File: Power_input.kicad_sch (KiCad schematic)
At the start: 10 parts, among them J12 DG390-5.0-02P

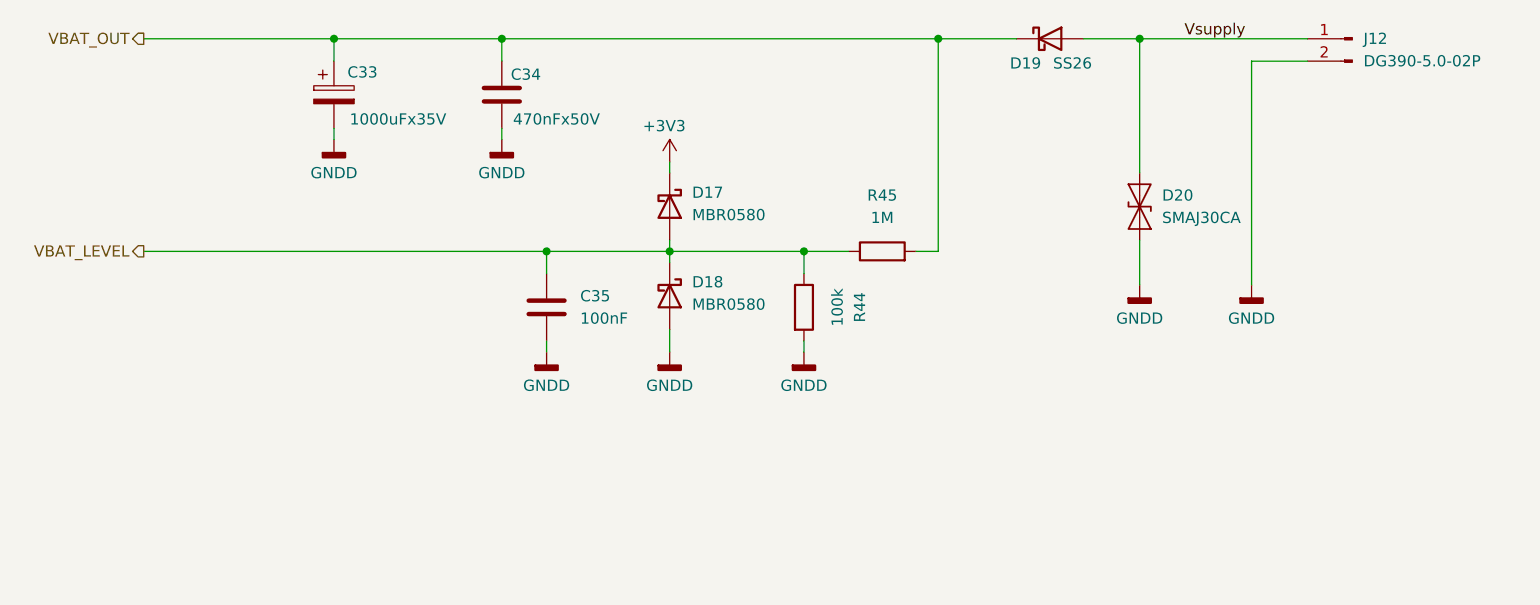
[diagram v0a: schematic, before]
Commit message: Dual SIM version
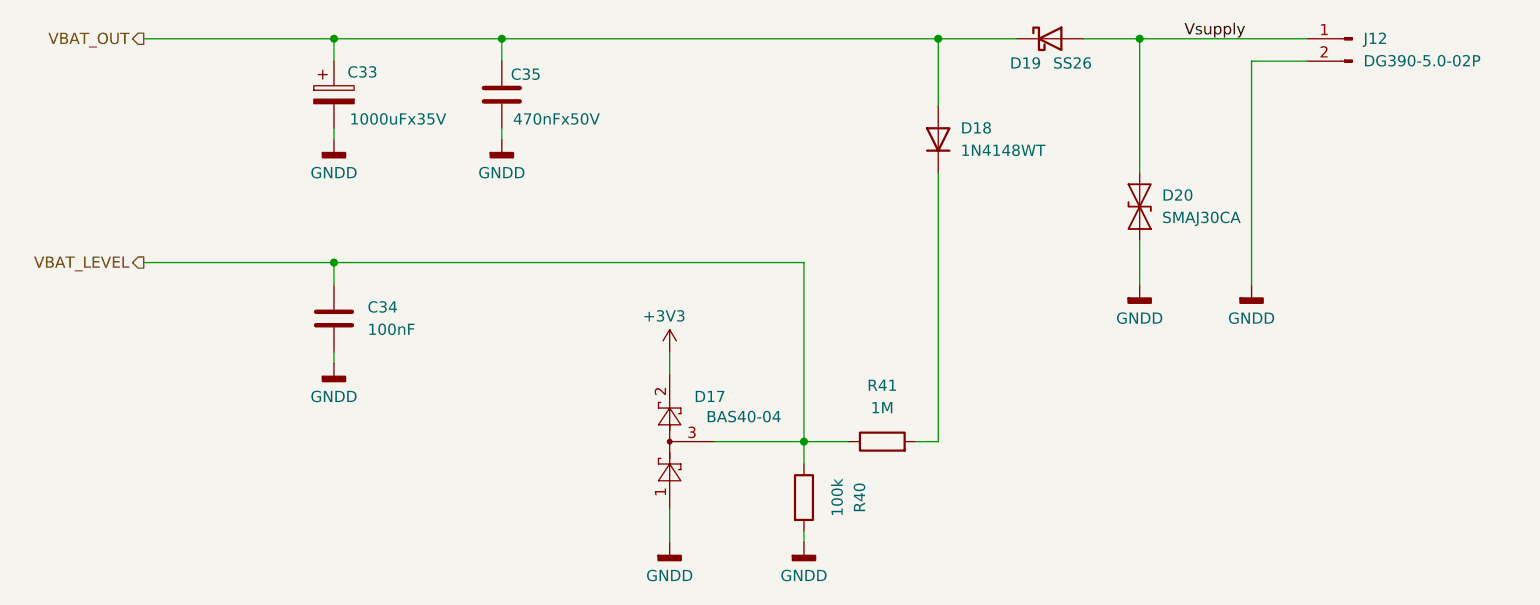
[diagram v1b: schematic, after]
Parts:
- removed D17, D18: MBR0580, Diode_SMD:D_SOD-123, symbol Diode:MBR0580
- added D17: BAS40-04, Package_TO_SOT_SMD:SOT-23, symbol Diode:BAS40-04
- added D18: 1N4148WT, Diode_SMD:D_SOD-523, symbol Diode:1N4148WT
- renumbered C35 to C34, C34 to C35, R44 to R40, R45 to R41
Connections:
- net +3V3: now also D17.2
- net GNDD: now also D17.1
- net VBAT_LEVEL: now also D17.3
- net VBAT_OUT: now also D18.2 (A); no longer R41.2
- new net: D18.1 (K), R41.2
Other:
- moved on the sheet: C34, R40, R41

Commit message: Replace SIM800C-DS with A7682E
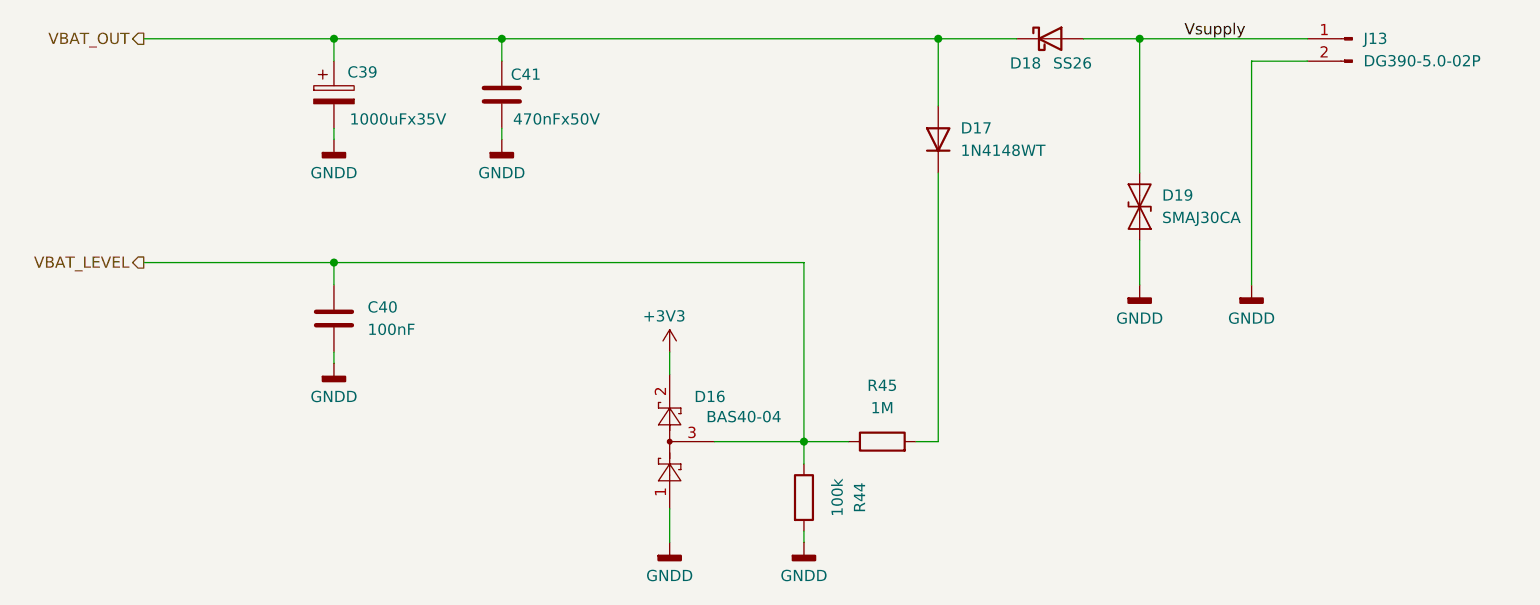
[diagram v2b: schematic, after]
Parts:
- renumbered C33 to C39, C34 to C40, C35 to C41, D17 to D16, D18 to D17, D19 to D18, D20 to D19, J12 to J13, R40 to R44, R41 to R45
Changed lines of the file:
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@@
 		(dnp no)
 		(fields_autoplaced yes)
-		(property "Reference" "#PWR080"
+		(property "Reference" "#PWR084"
 			(at 96.52 119.38 0)
 			(hide yes)
@@
 			(project "GSMreceiver"
 				(path "/bbc92722-7b85-49e8-a662-589426df605a/22f2c349-a150-4465-81d9-a52b1080446a"
-					(reference "#PWR080")
+					(reference "#PWR084")
 					(unit 1)
 				)
@@
 		(dnp no)
 		(fields_autoplaced yes)
-		(property "Reference" "R41"
+		(property "Reference" "R45"
 			(at 158.75 115.57 90)
 			(show_name no)
@@
 			(project "GSMreceiver"
 				(path "/bbc92722-7b85-49e8-a662-589426df605a/22f2c349-a150-4465-81d9-a52b1080446a"
-					(reference "R41")
+					(reference "R45")
 					(unit 1)
 				)
@@
 		(dnp no)
 		(fields_autoplaced yes)
-		(property "Reference" "J12"
+		(property "Reference" "J13"
 			(at 213.36 76.1999 0)
 			(show_name no)
@@
 			(project "GSMreceiver"
 				(path "/bbc92722-7b85-49e8-a662-589426df605a/22f2c349-a150-4465-81d9-a52b1080446a"
-					(reference "J12")
+					(reference "J13")
 					(unit 1)
 				)
@@
 		(dnp no)
 		(fields_autoplaced yes)
-		(property "Reference" "#PWR079"
+		(property "Reference" "#PWR083"
 			(at 96.52 93.98 0)
 			(hide yes)
@@
 			(project "GSMreceiver"
 				(path "/bbc92722-7b85-49e8-a662-589426df605a/22f2c349-a150-4465-81d9-a52b1080446a"
-					(reference "#PWR079")
+					(reference "#PWR083")
 					(unit 1)
 				)
@@
 		(dnp no)
 		(fields_autoplaced yes)
-		(property "Reference" "R40"
+		(property "Reference" "R44"
 			(at 156.21 128.27 90)
 			(show_name no)
@@
 			(project "GSMreceiver"
 				(path "/bbc92722-7b85-49e8-a662-589426df605a/22f2c349-a150-4465-81d9-a52b1080446a"
-					(reference "R40")
+					(reference "R44")
 					(unit 1)
 				)
@@
 		(in_pos_files yes)
 		(dnp no)
-		(property "Reference" "D17"
+		(property "Reference" "D16"
 			(at 140.97 116.84 90)
 			(show_name no)
@@
 			(project "GSMreceiver"
 				(path "/bbc92722-7b85-49e8-a662-589426df605a/22f2c349-a150-4465-81d9-a52b1080446a"
-					(reference "D17")
+					(reference "D16")
 					(unit 1)
 				)
@@
 		(dnp no)
 		(fields_autoplaced yes)
-		(property "Reference" "D18"
+		(property "Reference" "D17"
 			(at 167.64 86.3599 90)
 			(show_name no)
@@
 			(project "GSMreceiver"
 				(path "/bbc92722-7b85-49e8-a662-589426df605a/22f2c349-a150-4465-81d9-a52b1080446a"
-					(reference "D18")
+					(reference "D17")
 					(unit 1)
 				)
@@
 		(dnp no)
 		(fields_autoplaced yes)
-		(property "Reference" "#PWR085"
+		(property "Reference" "#PWR089"
 			(at 187.96 110.49 0)
 			(hide yes)
@@
 			(project "GSMreceiver"
 				(path "/bbc92722-7b85-49e8-a662-589426df605a/22f2c349-a150-4465-81d9-a52b1080446a"
-					(reference "#PWR085")
+					(reference "#PWR089")
 					(unit 1)
 				)
@@
 		(in_pos_files yes)
 		(dnp no)
-		(property "Reference" "#PWR082"
+		(property "Reference" "#PWR086"
 			(at 134.62 115.57 0)
 			(hide yes)
@@
 			(project "GSMreceiver"
 				(path "/bbc92722-7b85-49e8-a662-589426df605a/22f2c349-a150-4465-81d9-a52b1080446a"
-					(reference "#PWR082")
+					(reference "#PWR086")
 					(unit 1)
 				)
@@
 		(dnp no)
 		(fields_autoplaced yes)
-		(property "Reference" "#PWR086"
+		(property "Reference" "#PWR090"
 			(at 200.66 110.49 0)
 			(hide yes)
@@
 			(project "GSMreceiver"
 				(path "/bbc92722-7b85-49e8-a662-589426df605a/22f2c349-a150-4465-81d9-a52b1080446a"
-					(reference "#PWR086")
+					(reference "#PWR090")
 					(unit 1)
 				)
@@
 		(in_pos_files yes)
 		(dnp no)
-		(property "Reference" "C35"
+		(property "Reference" "C41"
 			(at 116.586 80.264 0)
 			(show_name no)
@@
 			(project "GSMreceiver"
 				(path "/bbc92722-7b85-49e8-a662-589426df605a/22f2c349-a150-4465-81d9-a52b1080446a"
-					(reference "C35")
+					(reference "C41")
 					(unit 1)
 				)
@@
 		(in_pos_files yes)
 		(dnp no)
-		(property "Reference" "D19"
+		(property "Reference" "D18"
 			(at 175.006 78.994 0)
 			(show_name no)
@@
 			(project "GSMreceiver"
 				(path "/bbc92722-7b85-49e8-a662-589426df605a/22f2c349-a150-4465-81d9-a52b1080446a"
-					(reference "D19")
+					(reference "D18")
 					(unit 1)
 				)
@@
 		(dnp no)
 		(fields_autoplaced yes)
-		(property "Reference" "#PWR083"
+		(property "Reference" "#PWR087"
 			(at 134.62 139.7 0)
 			(hide yes)
@@
 			(project "GSMreceiver"
 				(path "/bbc92722-7b85-49e8-a662-589426df605a/22f2c349-a150-4465-81d9-a52b1080446a"
-					(reference "#PWR083")
+					(reference "#PWR087")
 					(unit 1)
 				)
@@
 		(in_pos_files yes)
 		(dnp no)
-		(property "Reference" "C33"
+		(property "Reference" "C39"
 			(at 98.044 80.01 0)
 			(show_name no)
@@
 			(project "GSMreceiver"
 				(path "/bbc92722-7b85-49e8-a662-589426df605a/22f2c349-a150-4465-81d9-a52b1080446a"
-					(reference "C33")
+					(reference "C39")
 					(unit 1)
 				)
@@
 		(dnp no)
 		(fields_autoplaced yes)
-		(property "Reference" "C34"
+		(property "Reference" "C40"
 			(at 100.33 106.6799 0)
 			(show_name no)
@@
 			(project "GSMreceiver"
 				(path "/bbc92722-7b85-49e8-a662-589426df605a/22f2c349-a150-4465-81d9-a52b1080446a"
-					(reference "C34")
+					(reference "C40")
 					(unit 1)
 				)
@@
 		(dnp no)
 		(fields_autoplaced yes)
-		(property "Reference" "#PWR081"
+		(property "Reference" "#PWR085"
 			(at 115.57 93.98 0)
 			(hide yes)
@@
 			(project "GSMreceiver"
 				(path "/bbc92722-7b85-49e8-a662-589426df605a/22f2c349-a150-4465-81d9-a52b1080446a"
-					(reference "#PWR081")
+					(reference "#PWR085")
 					(unit 1)
 				)
@@
 		(dnp no)
 		(fields_autoplaced yes)
-		(property "Reference" "#PWR084"
+		(property "Reference" "#PWR088"
 			(at 149.86 139.7 0)
 			(hide yes)
@@
 			(project "GSMreceiver"
 				(path "/bbc92722-7b85-49e8-a662-589426df605a/22f2c349-a150-4465-81d9-a52b1080446a"
-					(reference "#PWR084")
+					(reference "#PWR088")
 					(unit 1)
 				)
@@
 		(dnp no)
 		(fields_autoplaced yes)
-		(property "Reference" "D20"
+		(property "Reference" "D19"
 			(at 190.5 93.9799 90)
 			(show_name no)
@@
 			(project "GSMreceiver"
 				(path "/bbc92722-7b85-49e8-a662-589426df605a/22f2c349-a150-4465-81d9-a52b1080446a"
-					(reference "D20")
-					(unit 1)
-				)
+					(reference "D19")
+					(unit 1)
+				)

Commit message: USB connector inversion fix
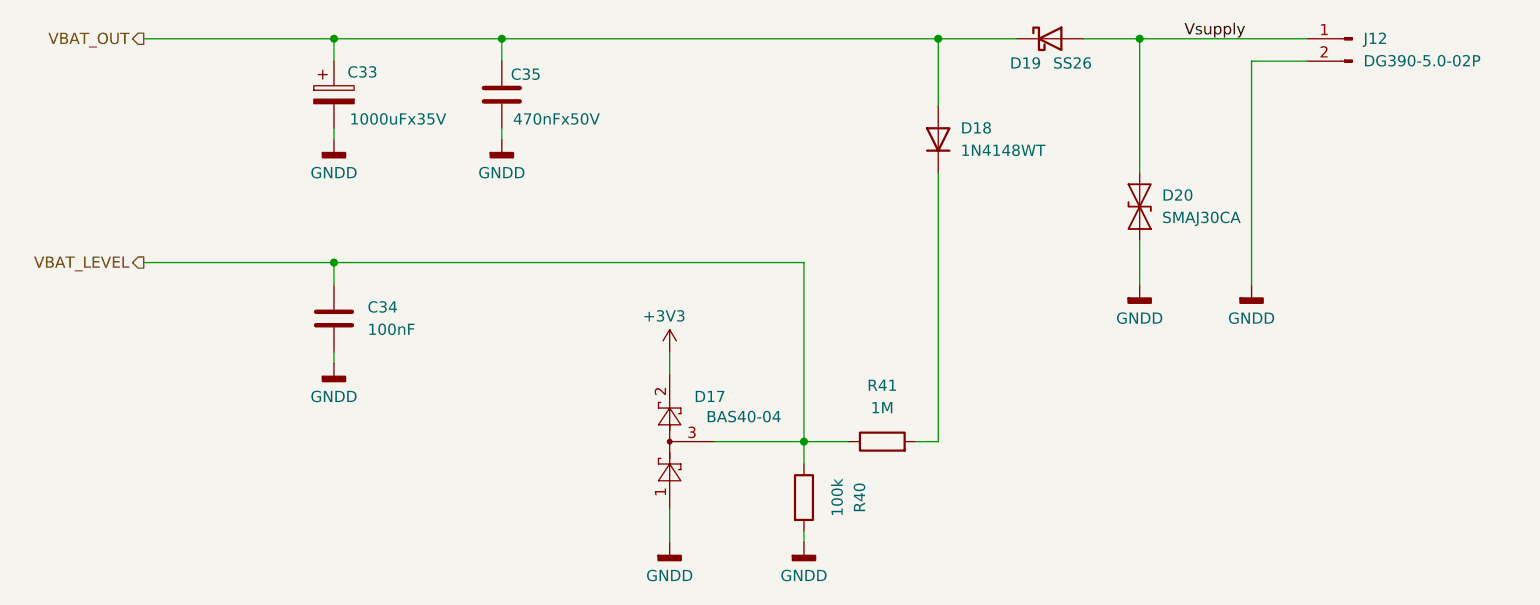
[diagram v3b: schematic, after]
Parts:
- renumbered C39 to C33, C40 to C34, C41 to C35, D16 to D17, D17 to D18, D18 to D19, D19 to D20, J13 to J12, R44 to R40, R45 to R41
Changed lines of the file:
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@@
 		(dnp no)
 		(fields_autoplaced yes)
-		(property "Reference" "#PWR084"
+		(property "Reference" "#PWR080"
 			(at 96.52 119.38 0)
 			(hide yes)
@@
 			(project "GSMreceiver"
 				(path "/bbc92722-7b85-49e8-a662-589426df605a/22f2c349-a150-4465-81d9-a52b1080446a"
-					(reference "#PWR084")
+					(reference "#PWR080")
 					(unit 1)
 				)
@@
 		(dnp no)
 		(fields_autoplaced yes)
-		(property "Reference" "R45"
+		(property "Reference" "R41"
 			(at 158.75 115.57 90)
 			(show_name no)
@@
 			(project "GSMreceiver"
 				(path "/bbc92722-7b85-49e8-a662-589426df605a/22f2c349-a150-4465-81d9-a52b1080446a"
-					(reference "R45")
+					(reference "R41")
 					(unit 1)
 				)
@@
 		(dnp no)
 		(fields_autoplaced yes)
-		(property "Reference" "J13"
+		(property "Reference" "J12"
 			(at 213.36 76.1999 0)
 			(show_name no)
@@
 			(project "GSMreceiver"
 				(path "/bbc92722-7b85-49e8-a662-589426df605a/22f2c349-a150-4465-81d9-a52b1080446a"
-					(reference "J13")
+					(reference "J12")
 					(unit 1)
 				)
@@
 		(dnp no)
 		(fields_autoplaced yes)
-		(property "Reference" "#PWR083"
+		(property "Reference" "#PWR079"
 			(at 96.52 93.98 0)
 			(hide yes)
@@
 			(project "GSMreceiver"
 				(path "/bbc92722-7b85-49e8-a662-589426df605a/22f2c349-a150-4465-81d9-a52b1080446a"
-					(reference "#PWR083")
+					(reference "#PWR079")
 					(unit 1)
 				)
@@
 		(dnp no)
 		(fields_autoplaced yes)
-		(property "Reference" "R44"
+		(property "Reference" "R40"
 			(at 156.21 128.27 90)
 			(show_name no)
@@
 			(project "GSMreceiver"
 				(path "/bbc92722-7b85-49e8-a662-589426df605a/22f2c349-a150-4465-81d9-a52b1080446a"
-					(reference "R44")
+					(reference "R40")
 					(unit 1)
 				)
@@
 		(in_pos_files yes)
 		(dnp no)
-		(property "Reference" "D16"
+		(property "Reference" "D17"
 			(at 140.97 116.84 90)
 			(show_name no)
@@
 			(project "GSMreceiver"
 				(path "/bbc92722-7b85-49e8-a662-589426df605a/22f2c349-a150-4465-81d9-a52b1080446a"
-					(reference "D16")
+					(reference "D17")
 					(unit 1)
 				)
@@
 		(dnp no)
 		(fields_autoplaced yes)
-		(property "Reference" "D17"
+		(property "Reference" "D18"
 			(at 167.64 86.3599 90)
 			(show_name no)
@@
 			(project "GSMreceiver"
 				(path "/bbc92722-7b85-49e8-a662-589426df605a/22f2c349-a150-4465-81d9-a52b1080446a"
-					(reference "D17")
+					(reference "D18")
 					(unit 1)
 				)
@@
 		(dnp no)
 		(fields_autoplaced yes)
-		(property "Reference" "#PWR089"
+		(property "Reference" "#PWR085"
 			(at 187.96 110.49 0)
 			(hide yes)
@@
 			(project "GSMreceiver"
 				(path "/bbc92722-7b85-49e8-a662-589426df605a/22f2c349-a150-4465-81d9-a52b1080446a"
-					(reference "#PWR089")
+					(reference "#PWR085")
 					(unit 1)
 				)
@@
 		(in_pos_files yes)
 		(dnp no)
-		(property "Reference" "#PWR086"
+		(property "Reference" "#PWR082"
 			(at 134.62 115.57 0)
 			(hide yes)
@@
 			(project "GSMreceiver"
 				(path "/bbc92722-7b85-49e8-a662-589426df605a/22f2c349-a150-4465-81d9-a52b1080446a"
-					(reference "#PWR086")
+					(reference "#PWR082")
 					(unit 1)
 				)
@@
 		(dnp no)
 		(fields_autoplaced yes)
-		(property "Reference" "#PWR090"
+		(property "Reference" "#PWR086"
 			(at 200.66 110.49 0)
 			(hide yes)
@@
 			(project "GSMreceiver"
 				(path "/bbc92722-7b85-49e8-a662-589426df605a/22f2c349-a150-4465-81d9-a52b1080446a"
-					(reference "#PWR090")
+					(reference "#PWR086")
 					(unit 1)
 				)
@@
 		(in_pos_files yes)
 		(dnp no)
-		(property "Reference" "C41"
+		(property "Reference" "C35"
 			(at 116.586 80.264 0)
 			(show_name no)
@@
 			(project "GSMreceiver"
 				(path "/bbc92722-7b85-49e8-a662-589426df605a/22f2c349-a150-4465-81d9-a52b1080446a"
-					(reference "C41")
+					(reference "C35")
 					(unit 1)
 				)
@@
 		(in_pos_files yes)
 		(dnp no)
-		(property "Reference" "D18"
+		(property "Reference" "D19"
 			(at 175.006 78.994 0)
 			(show_name no)
@@
 			(project "GSMreceiver"
 				(path "/bbc92722-7b85-49e8-a662-589426df605a/22f2c349-a150-4465-81d9-a52b1080446a"
-					(reference "D18")
+					(reference "D19")
 					(unit 1)
 				)
@@
 		(dnp no)
 		(fields_autoplaced yes)
-		(property "Reference" "#PWR087"
+		(property "Reference" "#PWR083"
 			(at 134.62 139.7 0)
 			(hide yes)
@@
 			(project "GSMreceiver"
 				(path "/bbc92722-7b85-49e8-a662-589426df605a/22f2c349-a150-4465-81d9-a52b1080446a"
-					(reference "#PWR087")
+					(reference "#PWR083")
 					(unit 1)
 				)
@@
 		(in_pos_files yes)
 		(dnp no)
-		(property "Reference" "C39"
+		(property "Reference" "C33"
 			(at 98.044 80.01 0)
 			(show_name no)
@@
 			(project "GSMreceiver"
 				(path "/bbc92722-7b85-49e8-a662-589426df605a/22f2c349-a150-4465-81d9-a52b1080446a"
-					(reference "C39")
+					(reference "C33")
 					(unit 1)
 				)
@@
 		(dnp no)
 		(fields_autoplaced yes)
-		(property "Reference" "C40"
+		(property "Reference" "C34"
 			(at 100.33 106.6799 0)
 			(show_name no)
@@
 			(project "GSMreceiver"
 				(path "/bbc92722-7b85-49e8-a662-589426df605a/22f2c349-a150-4465-81d9-a52b1080446a"
-					(reference "C40")
+					(reference "C34")
 					(unit 1)
 				)
@@
 		(dnp no)
 		(fields_autoplaced yes)
-		(property "Reference" "#PWR085"
+		(property "Reference" "#PWR081"
 			(at 115.57 93.98 0)
 			(hide yes)
@@
 			(project "GSMreceiver"
 				(path "/bbc92722-7b85-49e8-a662-589426df605a/22f2c349-a150-4465-81d9-a52b1080446a"
-					(reference "#PWR085")
+					(reference "#PWR081")
 					(unit 1)
 				)
@@
 		(dnp no)
 		(fields_autoplaced yes)
-		(property "Reference" "#PWR088"
+		(property "Reference" "#PWR084"
 			(at 149.86 139.7 0)
 			(hide yes)
@@
 			(project "GSMreceiver"
 				(path "/bbc92722-7b85-49e8-a662-589426df605a/22f2c349-a150-4465-81d9-a52b1080446a"
-					(reference "#PWR088")
+					(reference "#PWR084")
 					(unit 1)
 				)
@@
 		(dnp no)
 		(fields_autoplaced yes)
-		(property "Reference" "D19"
+		(property "Reference" "D20"
 			(at 190.5 93.9799 90)
 			(show_name no)
@@
 			(project "GSMreceiver"
 				(path "/bbc92722-7b85-49e8-a662-589426df605a/22f2c349-a150-4465-81d9-a52b1080446a"
-					(reference "D19")
-					(unit 1)
-				)
+					(reference "D20")
+					(unit 1)
+				)
